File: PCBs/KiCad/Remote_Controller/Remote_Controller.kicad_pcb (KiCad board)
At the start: 4 copper layers, 81 parts, among them J201 USB_C_Receptacle_USB2.0_16P, Q101 IRF7319, Q102 IRFML8244TRPBF, Q103 IRFML8244TRPBF, Q201 SS8050-G, Q202 SS8050-G, SW101 Power Switch, SW201 SW_Push, SW301 SW_Push, SW302 SW_Push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

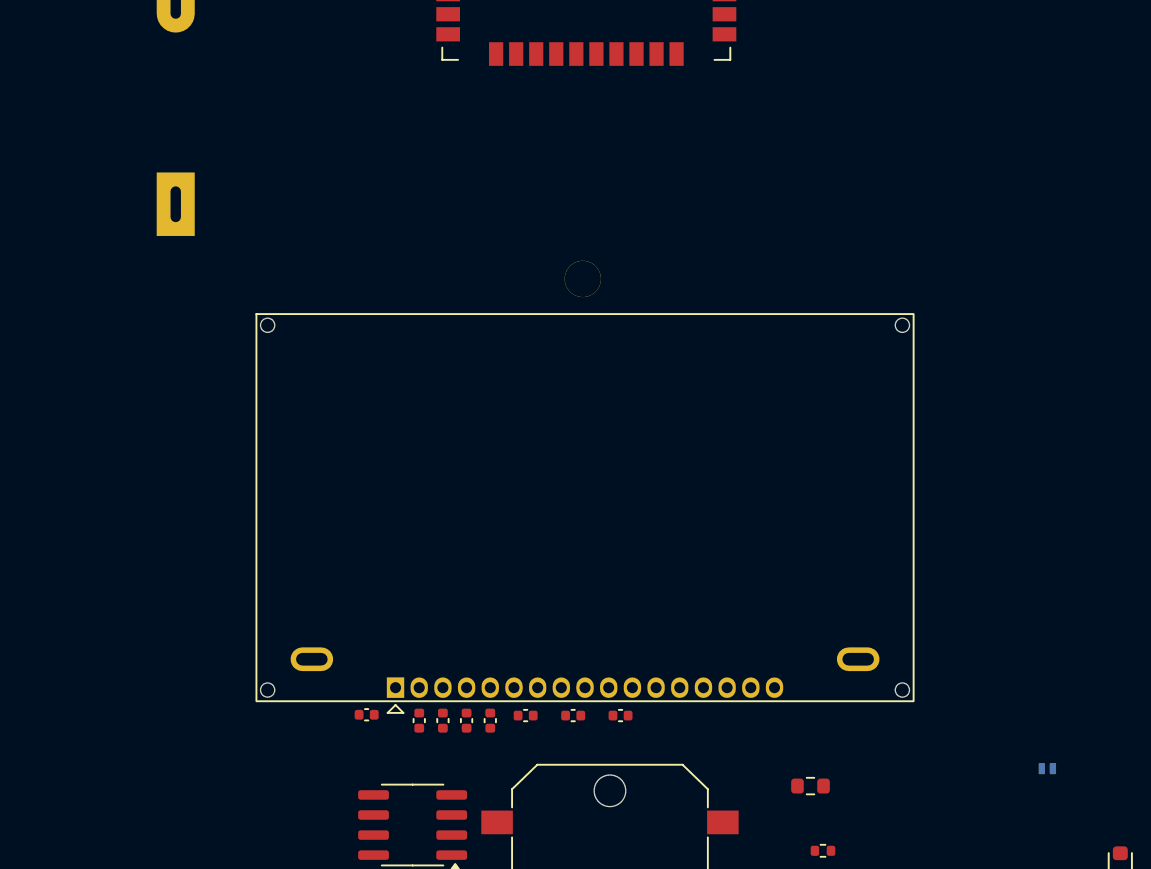
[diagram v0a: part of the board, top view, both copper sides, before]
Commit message: Added new symbol fields and completed BOM
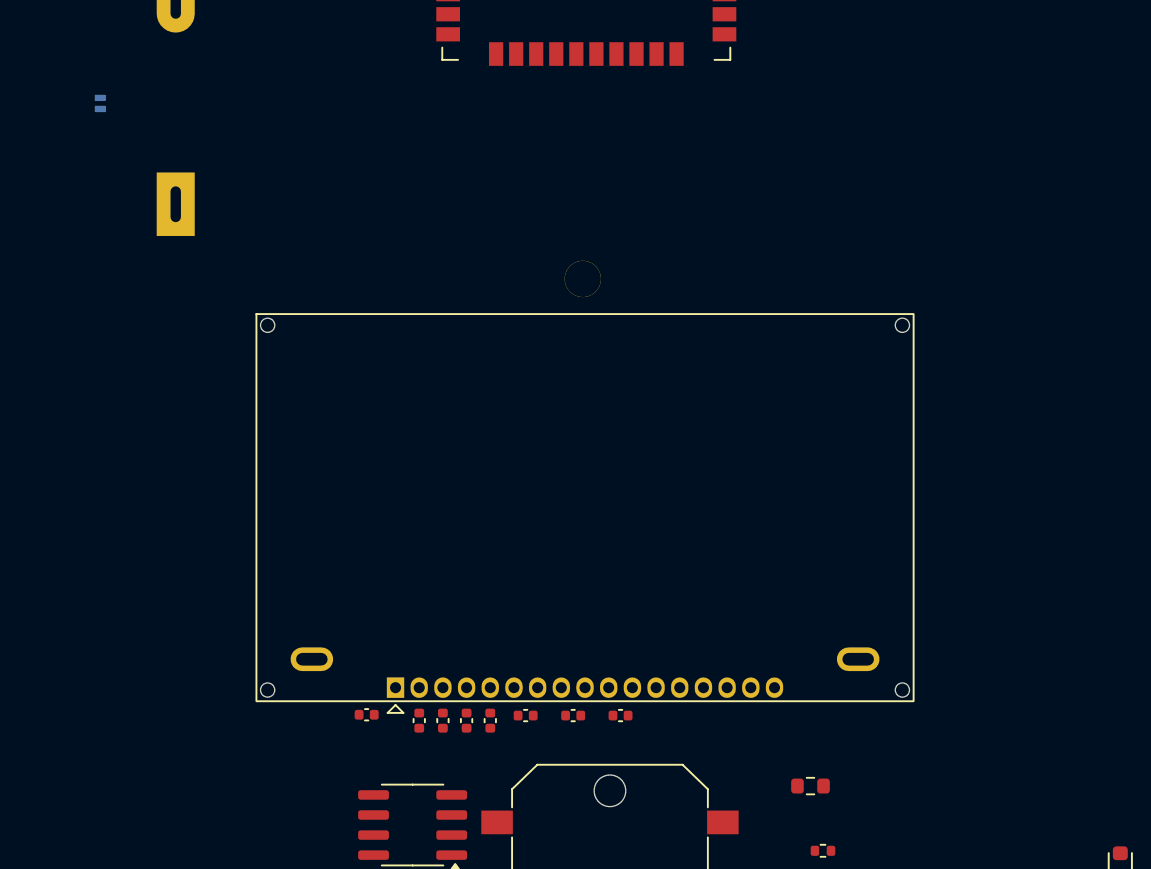
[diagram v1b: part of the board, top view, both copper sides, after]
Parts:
- moved D101 73.3 mm to (109.3, 69.3), turned to -90 degrees
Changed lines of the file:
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@@
 	(footprint "Diode_SMD:D_SOD-882"
 		(layer "B.Cu")
-		(at 169.28 111.4325 180)
+		(at 109.3 69.3 -90)
 		(descr "SOD-882, DFN1006-2, body 1.0 x 0.6 x 0.48mm, pitch 0.65mm, https://assets.nexperia.com/documents/package-information/SOD882.pdf")
 		(tags "Diode SOD882 DFN1006-2")
 		(property "Reference" "D101"
-			(at 0 1.35 0)
+			(at 0 1.35 90)
 			(layer "B.SilkS")
 			(hide yes)
@@
 		)
 		(property "Value" "P6SMB22CA"
-			(at 0 -1.35 0)
+			(at 0 -1.35 90)
 			(layer "B.Fab")
 			(hide yes)
@@
 		)
 		(property "Footprint" "Diode_SMD:D_SOD-882"
-			(at 0 0 0)
+			(at 0 0 90)
 			(unlocked yes)
 			(layer "B.Fab")
@@
 		)
 		(property "Datasheet" ""
-			(at 0 0 0)
+			(at 0 0 90)
 			(unlocked yes)
 			(layer "B.Fab")
@@
 		)
 		(property "Description" "Bidirectional transient-voltage-suppression diode"
-			(at 0 0 0)
+			(at 0 0 90)
 			(unlocked yes)
 			(layer "B.Fab")
@@
 		)
 		(fp_line
+			(start -0.81 -0.61)
+			(end -0.81 0.61)
+			(stroke
+				(width 0.12)
+				(type solid)
+			)
+			(layer "B.SilkS")
+		)
+		(fp_line
 			(start 0.5 -0.61)
 			(end -0.81 -0.61)
@@
 		)
 		(fp_line
-			(start -0.81 -0.61)
-			(end -0.81 0.61)
-			(stroke
-				(width 0.12)
-				(type solid)
-			)
-			(layer "B.SilkS")
-		)
-		(fp_line
 			(start 0.8 0.6)
 			(end -0.8 0.6)
@@
 		)
 		(fp_line
+			(start -0.8 -0.6)
+			(end -0.8 0.6)
+			(stroke
+				(width 0.05)
+				(type solid)
+			)
+			(layer "B.CrtYd")
+		)
+		(fp_line
+			(start -0.8 -0.6)
+			(end 0.8 -0.6)
+			(stroke
+				(width 0.05)
+				(type solid)
+			)
+			(layer "B.CrtYd")
+		)
+		(fp_line
 			(start 0.8 -0.6)
 			(end 0.8 0.6)
@@
 		)
 		(fp_line
-			(start -0.8 -0.6)
-			(end 0.8 -0.6)
-			(stroke
-				(width 0.05)
-				(type solid)
-			)
-			(layer "B.CrtYd")
-		)
-		(fp_line
-			(start -0.8 -0.6)
-			(end -0.8 0.6)
-			(stroke
-				(width 0.05)
-				(type solid)
-			)
-			(layer "B.CrtYd")
+			(start -0.5 0.3)
+			(end -0.5 -0.3)
+			(stroke
+				(width 0.1)
+				(type solid)
+			)
+			(layer "B.Fab")
 		)
 		(fp_line
@@
 		)
 		(fp_line
+			(start -0.15 0.2)
+			(end -0.15 -0.2)
+			(stroke
+				(width 0.1)
+				(type solid)
+			)
+			(layer "B.Fab")
+		)
+		(fp_line
+			(start 0.15 0.2)
+			(end 0.15 -0.2)
+			(stroke
+				(width 0.1)
+				(type solid)
+			)
+			(layer "B.Fab")
+		)
+		(fp_line
+			(start -0.3 0)
+			(end -0.15 0)
+			(stroke
+				(width 0.1)
+				(type solid)
+			)
+			(layer "B.Fab")
+		)
+		(fp_line
+			(start -0.15 0)
+			(end 0.15 0.2)
+			(stroke
+				(width 0.1)
+				(type solid)
+			)
+			(layer "B.Fab")
+		)
+		(fp_line
+			(start 0.3 0)
+			(end 0.15 0)
+			(stroke
+				(width 0.1)
+				(type solid)
+			)
+			(layer "B.Fab")
+		)
+		(fp_line
+			(start 0.15 -0.2)
+			(end -0.15 0)
+			(stroke
+				(width 0.1)
+				(type solid)
+			)
+			(layer "B.Fab")
+		)
+		(fp_line
+			(start -0.5 -0.3)
+			(end 0.5 -0.3)
+			(stroke
+				(width 0.1)
+				(type solid)
+			)
+			(layer "B.Fab")
+		)
+		(fp_line
 			(start 0.5 -0.3)
 			(end 0.5 0.3)
@@
 			(layer "B.Fab")
 		)
-		(fp_line
-			(start 0.3 0)
-			(end 0.15 0)
-			(stroke
-				(width 0.1)
-				(type solid)
-			)
-			(layer "B.Fab")
-		)
-		(fp_line
-			(start 0.15 0.2)
-			(end 0.15 -0.2)
-			(stroke
-				(width 0.1)
-				(type solid)
-			)
-			(layer "B.Fab")
-		)
-		(fp_line
-			(start 0.15 -0.2)
-			(end -0.15 0)
-			(stroke
-				(width 0.1)
-				(type solid)
-			)
-			(layer "B.Fab")
-		)
-		(fp_line
-			(start -0.15 0.2)
-			(end -0.15 -0.2)
-			(stroke
-				(width 0.1)
-				(type solid)
-			)
-			(layer "B.Fab")
-		)
-		(fp_line
-			(start -0.15 0)
-			(end 0.15 0.2)
-			(stroke
-				(width 0.1)
-				(type solid)
-			)
-			(layer "B.Fab")
-		)
-		(fp_line
-			(start -0.3 0)
-			(end -0.15 0)
-			(stroke
-				(width 0.1)
-				(type solid)
-			)
-			(layer "B.Fab")
-		)
-		(fp_line
-			(start -0.5 0.3)
-			(end -0.5 -0.3)
-			(stroke
-				(width 0.1)
-				(type solid)
-			)
-			(layer "B.Fab")
-		)
-		(fp_line
-			(start -0.5 -0.3)
-			(end 0.5 -0.3)
-			(stroke
-				(width 0.1)
-				(type solid)
-			)
-			(layer "B.Fab")
-		)
 		(fp_text user "${REFERENCE}"
-			(at -0.127 1.35 0)
+			(at -0.127 1.35 90)
 			(layer "B.Fab")
 			(effects
@@
 		)
 		(pad "" smd roundrect
-			(at -0.35 0 180)
+			(at -0.35 0 270)
 			(size 0.3 0.6)
 			(layers "B.Paste")
@@
 		)
 		(pad "" smd roundrect
-			(at 0.35 0 180)
+			(at 0.35 0 270)
 			(size 0.3 0.6)
 			(layers "B.Paste")
@@
 		)
 		(pad "1" smd roundrect
-			(at -0.35 0 180)
+			(at -0.35 0 270)
 			(size 0.4 0.7)
 			(layers "B.Cu" "B.Mask")
@@
 		)
 		(pad "2" smd roundrect
-			(at 0.35 0 180)
+			(at 0.35 0 270)
 			(size 0.4 0.7)
 			(layers "B.Cu" "B.Mask")
